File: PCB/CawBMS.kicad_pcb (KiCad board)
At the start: 4 copper layers, 53.5 x 38 mm, 131 parts, among them CN3 SPI, CN4 USART, CN5 SWD, CN6 WAFER-SH1.0-6PWB, Q1 CSD13381F4, Q10 TP0610K-T1-GE3, Q2 CSD13381F4, Q3 CSD13381F4, Q4 CSD13381F4, Q5 CSD13381F4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

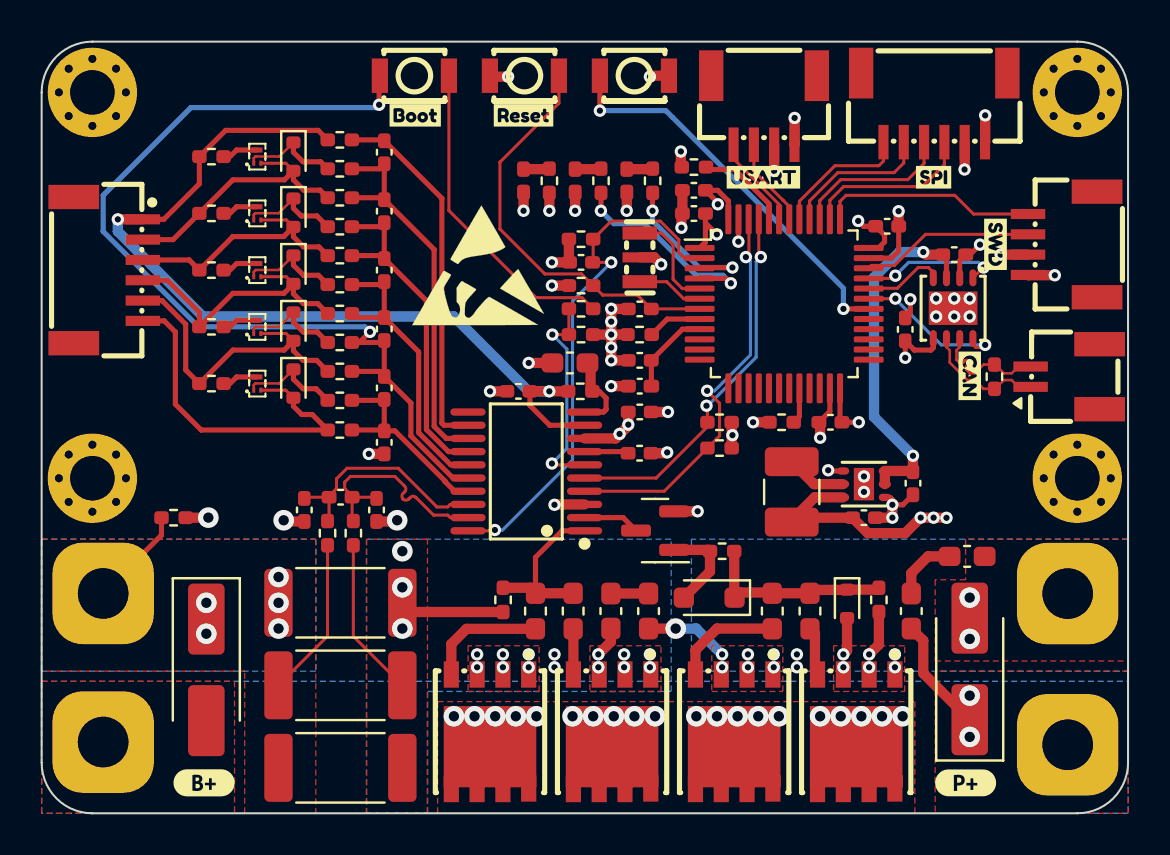
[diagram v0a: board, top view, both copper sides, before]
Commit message: 修复充电MOS无法开启的问题
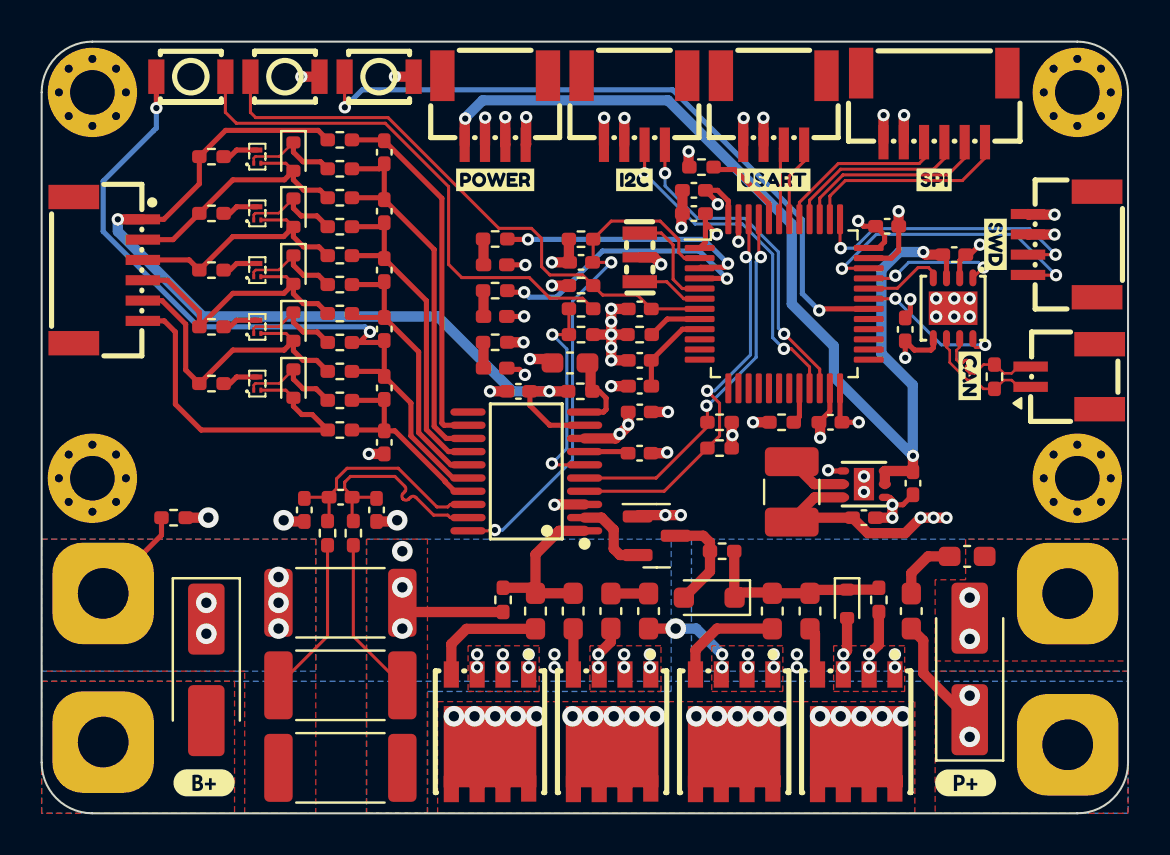
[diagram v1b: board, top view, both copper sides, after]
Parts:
- removed the REF** at (131.5, 103.0)
- removed kibuzzard-6577EB0A: G***, kibuzzard-6577EB0A
- removed kibuzzard-6577EB11: G***, kibuzzard-6577EB11
- added CN1: SWD, Rick_Connector:CONN-SMD_4P-P1.00_WAFER-SH1.0-4PWB, F.Cu at (132.3, 95.4)
- added CN2: I2C, Rick_Connector:CONN-SMD_4P-P1.00_WAFER-SH1.0-4PWB, F.Cu at (139.2, 95.4)
- added kibuzzard-658FE662: G***, kibuzzard-658FE662, F.Cu at (139.2, 98.8)
- added kibuzzard-658FE679: G***, kibuzzard-658FE679, F.Cu at (132.3, 98.8)
- moved SW2 12.6 mm to (126.6, 93.7)
- moved SW1 11.8 mm to (122.0, 93.7), turned to 180 degrees
- moved SW3 11.0 mm to (117.3, 93.7)
- moved D3 9.33 mm to (132.3, 108.1), turned to 0 degrees
- moved R10 8.39 mm to (132.3, 106.8), turned to 0 degrees
- moved R7 8.27 mm to (132.3, 101.7), turned to 0 degrees
- moved D2 7.76 mm to (132.3, 105.5), turned to 0 degrees
- moved D1 7.69 mm to (132.3, 103.0), turned to 0 degrees
- moved R9 7.51 mm to (132.3, 104.3), turned to 0 degrees
- moved kibuzzard-6577EBAB 0.52 mm to (146.1, 98.8)
- moved CN4 0.48 mm to (146.1, 95.4)
- moved R2 0.37 mm to (142.5, 98.2)
- moved Q10 0.27 mm to (140.3, 116.3), turned to 0 degrees
- moved kibuzzard-6577EBC9 0.13 mm to (153.9, 98.8)
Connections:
- CN3 pad 1: +3.3V -> /SPI1_NSS
- CN3 pad 2: GND -> /SPI1_SCK
- CN3 pad 3: /SPI1_NSS -> /SPI1_MISO
- CN3 pad 4: /SPI1_SCK -> /SPI1_MOSI
- CN3 pad 5: /SPI1_MISO -> GND
- CN3 pad 6: /SPI1_MOSI -> +3.3V
- CN4 pad 1: +3.3V -> /USART1_TX
- CN4 pad 2: GND -> /USART1_RX
- CN4 pad 3: /USART1_TX -> GND
- CN4 pad 4: /USART1_RX -> +3.3V
- CN5 pad 1: +3.3V -> /SWDIO
- CN5 pad 2: GND -> /SWCLK
- CN5 pad 3: /SWDIO -> GND
- CN5 pad 4: /SWCLK -> +3.3V
- Q10 pad 1: Net-(D11-A) -> GND
- Q10 pad 2: GND -> /BQ76920/CHG
- Q10 pad 3: /BQ76920/CHG -> Net-(D11-A)
- U1 pad 21: unconnected-(U1-PB10-Pad21) -> /I2C2_SCL
- U1 pad 22: unconnected-(U1-PB11-Pad22) -> /I2C2_SDA
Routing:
- net +5V: track 17.6 -> 51.5 mm, vias 2 -> 3
- net /I2C2_SCL: track 0.00 -> 16.9 mm, vias 0 -> 2
- net /I2C2_SDA: track 0.00 -> 16.5 mm, vias 0 -> 2
- net /KEY_A: track 19.6 -> 34.3 mm
- net Net-(R29-Pad1): track 15.7 -> 26.1 mm
- net /BQ76920/VC1: track 47.2 -> 37.2 mm
- net /RESET: track 20.2 -> 28.7 mm
- net /SWDIO: track 8.54 -> 14.8 mm, vias 0 -> 2
- net /LED_A: track 7.90 -> 12.9 mm
- net GND: track 43.5 -> 48.4 mm, vias 41 -> 45
- net /SWCLK: track 10.6 -> 14.3 mm, vias 0 -> 2
- net /LED_B: track 10.4 -> 13.8 mm
- net +3.3V: track 39.4 -> 42.2 mm, vias 20 -> 22
- net /SPI1_NSS: track 8.41 -> 10.3 mm
- net /SPI1_SCK: track 7.86 -> 9.78 mm
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
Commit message: 调整丝印 📐
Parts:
- removed kibuzzard-6577F385: G***, kibuzzard-6577F385
- added kibuzzard-65902364: G***, kibuzzard-65902364, B.Cu at (129.0, 110.5)
